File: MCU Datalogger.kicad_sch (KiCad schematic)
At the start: 25 parts, among them U1 24LC1025, U2 24LC1025, U3 DS1337S+, U4 ATMEGA328P-AU, Y1 32.768KHz, Y2 16MHz

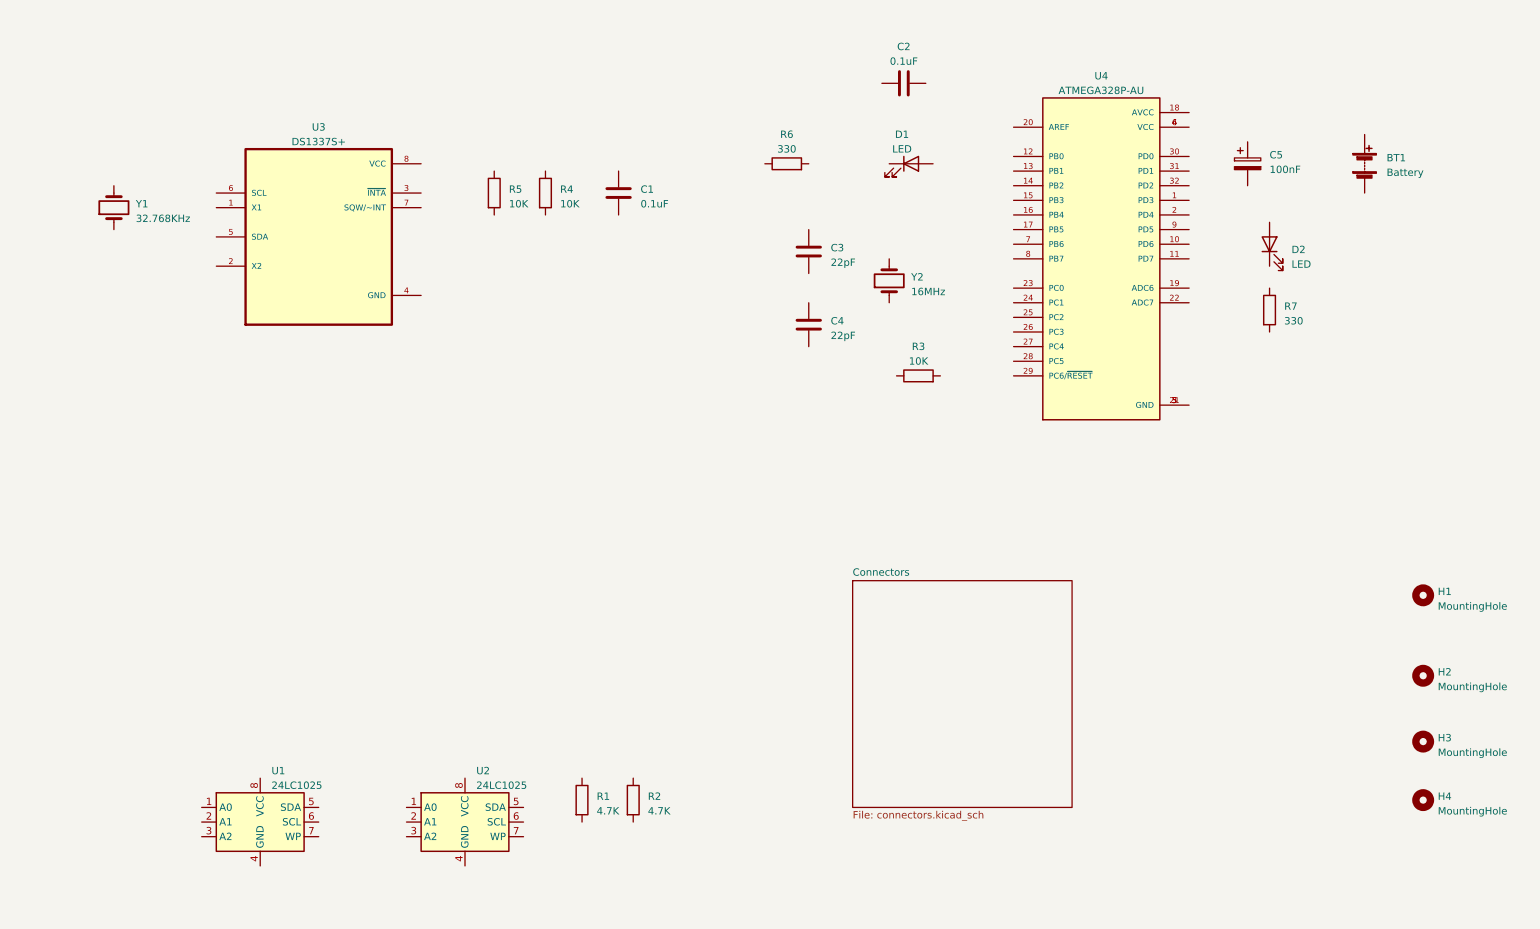
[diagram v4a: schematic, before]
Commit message: Completed wiring of main sheet
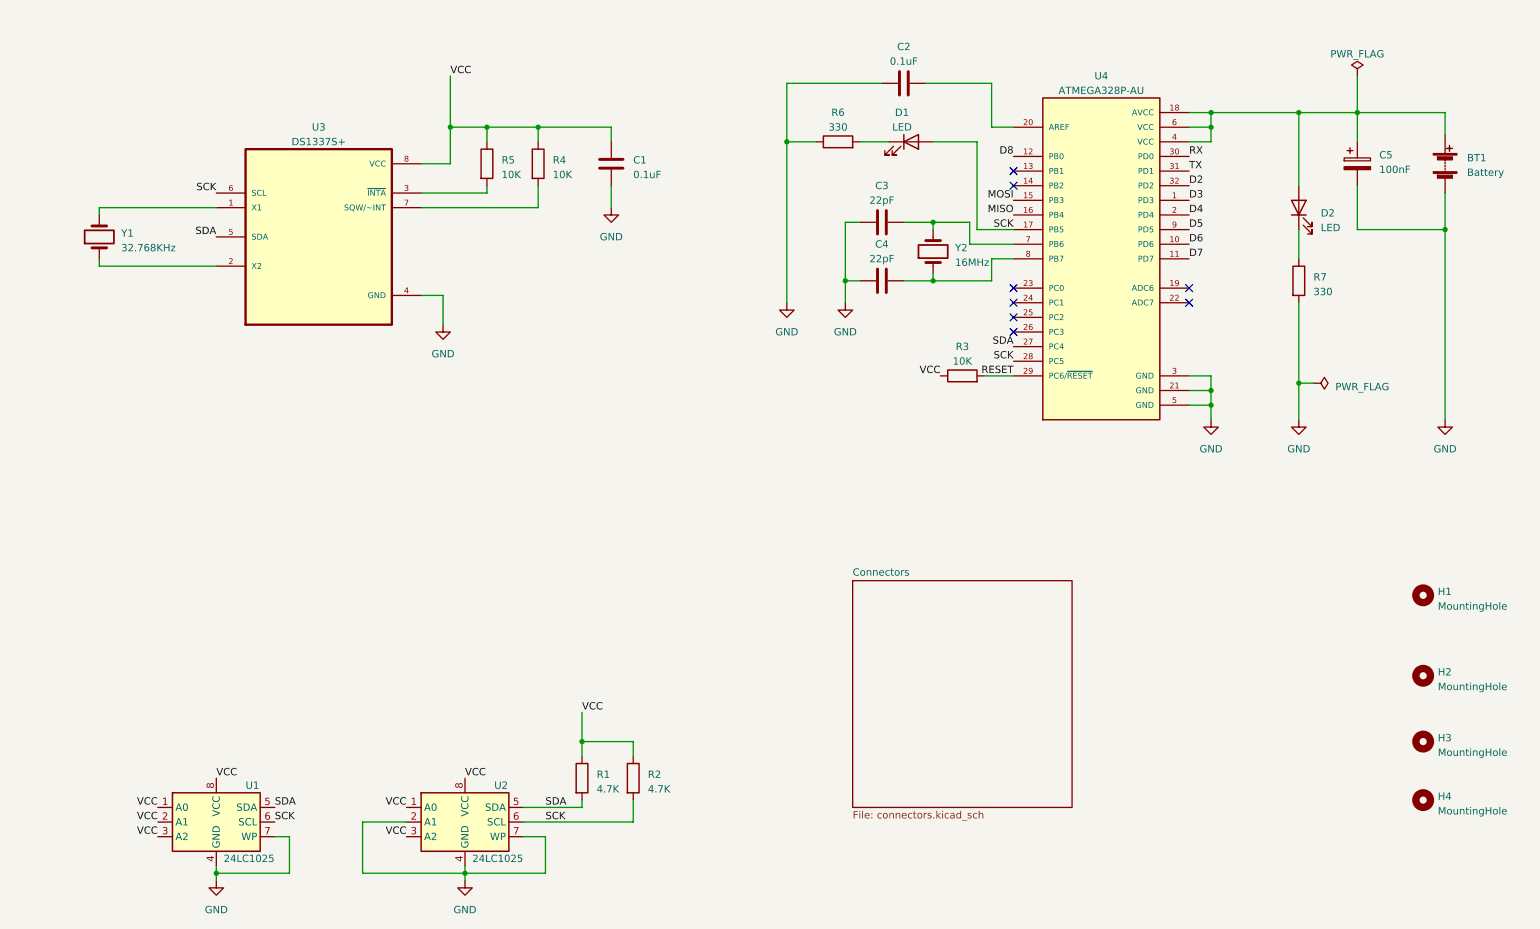
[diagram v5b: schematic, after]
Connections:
- net VCC: now reaches R5.1
- net VCC: now also C1.1, R1.1, R2.1, R3.1, R4.1, U1.1 (A0), U1.2 (A1), U1.3 (A2), U1.8 (VCC), U2.1 (A0), U2.3 (A2), U2.8 (VCC), U3.8 (VCC)
- net at R5.2: now also U3.3 (~{INTA})
- net GND: now reaches C3.1
- net GND: now also BT1.2 (-), C1.2, C2.1, C4.1, C5.2, R6.1, R7.2, U1.4 (GND), U1.7 (WP), U2.2 (A1), U2.4 (GND), U2.7 (WP), U3.4 (GND), U4.21 (GND), U4.3 (GND), U4.5 (GND)
- net at C3.2: now also U4.7 (PB6), Y2.2
- net at R7.1: now also D2.1 (K)
- net at D2.2 (A): now also BT1.1 (+), C5.1, U4.18 (AVCC), U4.4 (VCC), U4.6 (VCC)
- net SDA: now reaches R1.2
- net SDA: now also U1.5 (SDA), U2.5 (SDA), U3.5 (SDA), U4.27 (PC4)
- net SCK: now reaches R2.2
- net SCK: now also D1.2 (A), U1.6 (SCL), U2.6 (SCL), U3.6 (SCL), U4.17 (PB5), U4.28 (PC5)
- net at D1.1 (K): now also R6.2
- net at Y1.1: now also U3.2 (X2)
- net at Y1.2: now also U3.1 (X1)
- net at U3.7 (SQW/~INT): now also R4.2
- net RESET: now reaches R3.2
- net RESET: now also U4.29 (PC6/~{RESET})
- net D3: now reaches U4.1 (PD3)
- net D6: now reaches U4.10 (PD6)
- net D7: now reaches U4.11 (PD7)
- net D8: now reaches U4.12 (PB0)
- net MOSI: now reaches U4.15 (PB3)
- net MISO: now reaches U4.16 (PB4)
- net D4: now reaches U4.2 (PD4)
- net at U4.20 (AREF): now also C2.2
- net RX: now reaches U4.30 (PD0)
- net TX: now reaches U4.31 (PD1)
- net D2: now reaches U4.32 (PD2)
- net at U4.8 (PB7): now also C4.2, Y2.1
- net D5: now reaches U4.9 (PD5)
- no-connect marks 0 -> 8
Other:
- moved on the sheet: BT1, C1, C3, C4, C5, D1, D2, R1, R2, R3, R4, R5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

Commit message: Completed wiring in the second sheet.
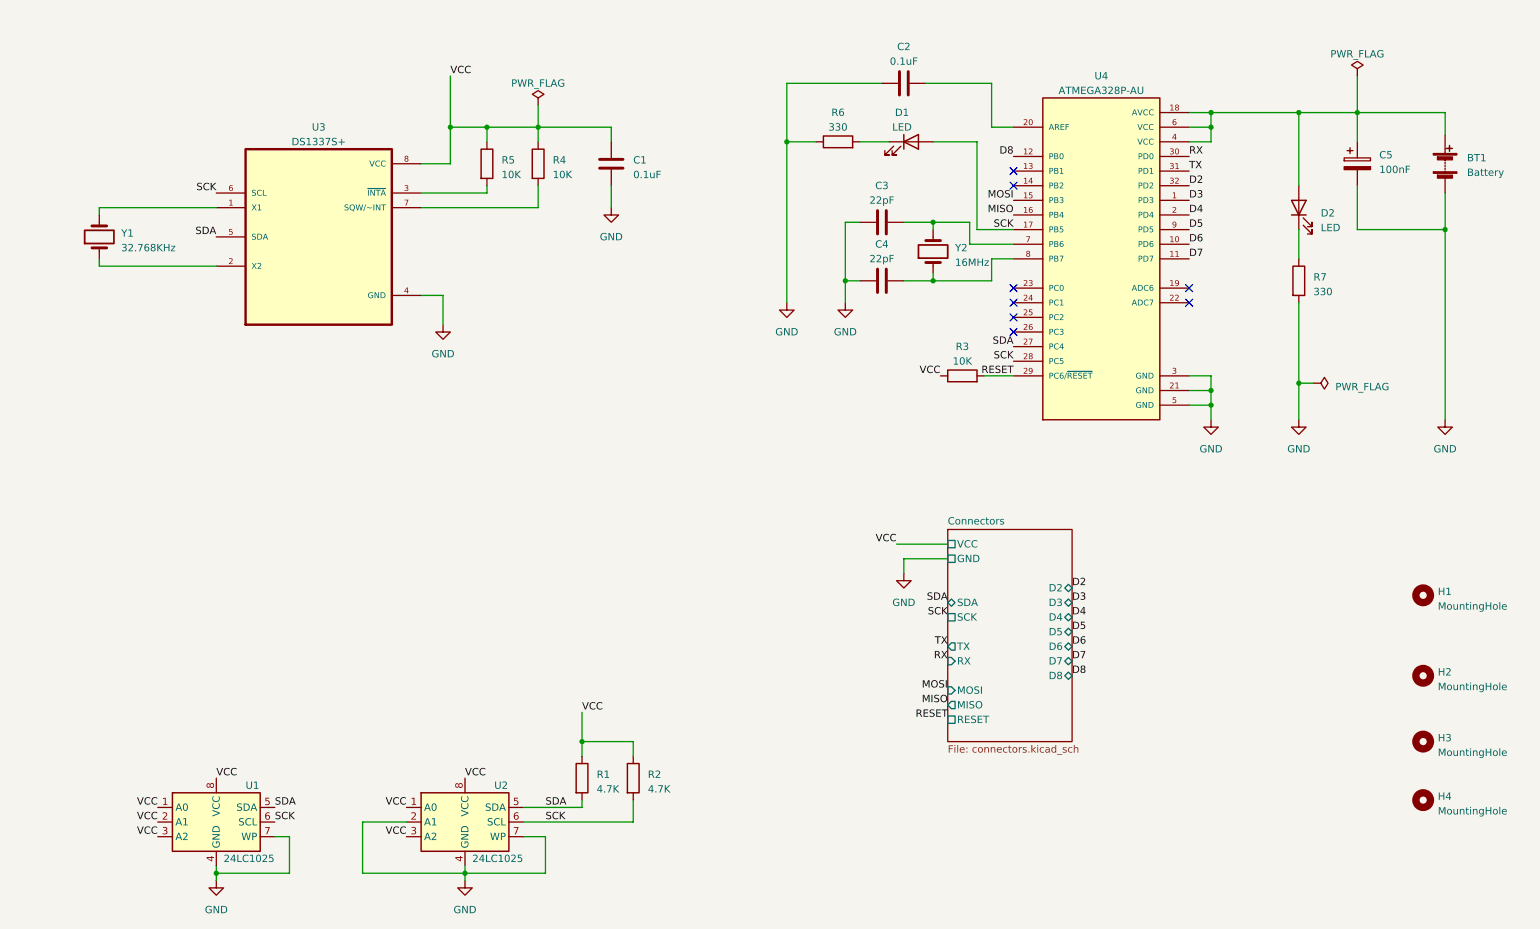
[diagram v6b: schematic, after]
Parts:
- U4: footprint Footprints:QFP80P900X900X120-32N -> QFP80P900X900X120-32N
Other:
- sheet Connectors ports: added D2, D3, D4, D5, D6, D7, D8, GND, MISO, MOSI, RESET, RX, SCK, SDA, TX, VCC; removed none
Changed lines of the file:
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@@
+    (stroke (width 0) (type default))
+  )
+  (wire (pts (xy 109.22 33.02) (xy 109.22 36.83))
     (stroke (width 0) (type default))
   )
@@
     (stroke (width 0) (type default))
   )
+  (wire (pts (xy 88.9 43.18) (xy 93.98 43.18))
+    (stroke (width 0) (type default))
+  )
   (wire (pts (xy 226.06 34.29) (xy 222.25 34.29))
     (stroke (width 0) (type default))
@@
     (stroke (width 0) (type default))
   )
+  (wire (pts (xy 172.72 111.76) (xy 172.72 114.3))
+    (stroke (width 0) (type default))
+  )
   (wire (pts (xy 241.3 34.29) (xy 226.06 34.29))
     (stroke (width 0) (type default))
@@
     (stroke (width 0) (type default))
   )
+  (wire (pts (xy 180.34 111.76) (xy 172.72 111.76))
+    (stroke (width 0) (type default))
+  )
   (wire (pts (xy 106.68 160.02) (xy 110.49 160.02))
     (stroke (width 0) (type default))
@@
     (stroke (width 0) (type default))
   )
-  (wire (pts (xy 88.9 43.18) (xy 93.98 43.18))
-    (stroke (width 0) (type default))
-  )
   (wire (pts (xy 152.4 29.21) (xy 152.4 39.37))
     (stroke (width 0) (type default))
@@
     (stroke (width 0) (type default))
   )
+  (wire (pts (xy 171.45 109.22) (xy 180.34 109.22))
+    (stroke (width 0) (type default))
+  )
   (wire (pts (xy 33.02 50.8) (xy 33.02 52.07))
     (stroke (width 0) (type default))
@@
     (stroke (width 0) (type default))
   )
+  (label "MOSI" (at 180.34 134.62 180) (fields_autoplaced)
+    (effects (font (size 1.27 1.27)) (justify right bottom))
+  )
   (label "D2" (at 222.25 46.99 0) (fields_autoplaced)
     (effects (font (size 1.27 1.27)) (justify left bottom))
@@
     (effects (font (size 1.27 1.27)) (justify right bottom))
   )
+  (label "VCC" (at 171.45 109.22 180) (fields_autoplaced)
+    (effects (font (size 1.27 1.27)) (justify right bottom))
+  )
   (label "SCK" (at 191.77 54.61 180) (fields_autoplaced)
     (effects (font (size 1.27 1.27)) (justify right bottom))
@@
     (effects (font (size 1.27 1.27)) (justify right bottom))
   )
+  (label "D7" (at 201.93 129.54 0) (fields_autoplaced)
+    (effects (font (size 1.27 1.27)) (justify left bottom))
+  )
   (label "SDA" (at 110.49 154.94 0) (fields_autoplaced)
     (effects (font (size 1.27 1.27)) (justify left bottom))
   )
+  (label "D3" (at 201.93 119.38 0) (fields_autoplaced)
+    (effects (font (size 1.27 1.27)) (justify left bottom))
+  )
   (label "RESET" (at 191.77 80.01 180) (fields_autoplaced)
     (effects (font (size 1.27 1.27)) (justify right bottom))
@@
     (effects (font (size 1.27 1.27)) (justify right bottom))
   )
+  (label "RX" (at 180.34 129.54 180) (fields_autoplaced)
+    (effects (font (size 1.27 1.27)) (justify right bottom))
+  )
   (label "RX" (at 222.25 41.91 0) (fields_autoplaced)
     (effects (font (size 1.27 1.27)) (justify left bottom))
@@
     (effects (font (size 1.27 1.27)) (justify left bottom))
   )
+  (label "D2" (at 201.93 116.84 0) (fields_autoplaced)
+    (effects (font (size 1.27 1.27)) (justify left bottom))
+  )
   (label "SDA" (at 63.5 154.94 0) (fields_autoplaced)
     (effects (font (size 1.27 1.27)) (justify left bottom))
@@
     (effects (font (size 1.27 1.27)) (justify left bottom))
   )
+  (label "D6" (at 201.93 127 0) (fields_autoplaced)
+    (effects (font (size 1.27 1.27)) (justify left bottom))
+  )
   (label "SCK" (at 63.5 157.48 0) (fields_autoplaced)
     (effects (font (size 1.27 1.27)) (justify left bottom))
@@
     (effects (font (size 1.27 1.27)) (justify right bottom))
   )
+  (label "SCK" (at 180.34 121.92 180) (fields_autoplaced)
+    (effects (font (size 1.27 1.27)) (justify right bottom))
+  )
   (label "VCC" (at 53.34 149.86 0) (fields_autoplaced)
     (effects (font (size 1.27 1.27)) (justify left bottom))
   )
+  (label "SDA" (at 180.34 119.38 180) (fields_autoplaced)
+    (effects (font (size 1.27 1.27)) (justify right bottom))
+  )
+  (label "D5" (at 201.93 124.46 0) (fields_autoplaced)
+    (effects (font (size 1.27 1.27)) (justify left bottom))
+  )
+  (label "D8" (at 201.93 132.08 0) (fields_autoplaced)
+    (effects (font (size 1.27 1.27)) (justify left bottom))
+  )
+  (label "RESET" (at 180.34 139.7 180) (fields_autoplaced)
+    (effects (font (size 1.27 1.27)) (justify right bottom))
+  )
+  (label "D4" (at 201.93 121.92 0) (fields_autoplaced)
+    (effects (font (size 1.27 1.27)) (justify left bottom))
+  )
   (label "D5" (at 222.25 54.61 0) (fields_autoplaced)
     (effects (font (size 1.27 1.27)) (justify left bottom))
@@
     (effects (font (size 1.27 1.27)) (justify right bottom))
   )
+  (label "MISO" (at 180.34 137.16 180) (fields_autoplaced)
+    (effects (font (size 1.27 1.27)) (justify right bottom))
+  )
+  (label "TX" (at 180.34 127 180) (fields_autoplaced)
+    (effects (font (size 1.27 1.27)) (justify right bottom))
+  )
   (label "VCC" (at 179.07 80.01 180) (fields_autoplaced)
     (effects (font (size 1.27 1.27)) (justify right bottom))
@@
         (path "/a2e2aee7-f3a1-41aa-a08b-33521bd80092"
           (reference "C3") (unit 1)
+        )
+      )
+    )
+  )
+  (symbol (lib_id "power:PWR_FLAG") (at 109.22 33.02 0) (unit 1)
+    (in_bom yes) (on_board yes) (dnp no) (fields_autoplaced)
+    (property "Reference" "#FLG03" (at 109.22 31.115 0)
+      (effects (font (size 1.27 1.27)) hide)
+    )
+    (property "Value" "PWR_FLAG" (at 109.22 29.21 0)
+      (effects (font (size 1.27 1.27)))
+    )
+    (property "Footprint" "" (at 109.22 33.02 0)
+      (effects (font (size 1.27 1.27)) hide)
+    )
+    (property "Datasheet" "~" (at 109.22 33.02 0)
+      (effects (font (size 1.27 1.27)) hide)
+    )
+    (pin "1")
+    (instances
+      (project "MCU Datalogger"
+        (path "/a2e2aee7-f3a1-41aa-a08b-33521bd80092"
+          (reference "#FLG03") (unit 1)
         )
       )
@@
         (path "/a2e2aee7-f3a1-41aa-a08b-33521bd80092"
           (reference "R1") (unit 1)
+        )
+      )
+    )
+  )
+  (symbol (lib_id "power:GND") (at 172.72 114.3 0) (unit 1)
+    (in_bom yes) (on_board yes) (dnp no) (fields_autoplaced)
+    (property "Reference" "#PWR010" (at 172.72 120.65 0)
+      (effects (font (size 1.27 1.27)) hide)
+    )
+    (property "Value" "GND" (at 172.72 119.38 0)
+      (effects (font (size 1.27 1.27)))
+    )
+    (property "Footprint" "" (at 172.72 114.3 0)
+      (effects (font (size 1.27 1.27)) hide)
+    )
+    (property "Datasheet" "" (at 172.72 114.3 0)
+      (effects (font (size 1.27 1.27)) hide)
+    )
+    (pin "1")
+    (instances
+      (project "MCU Datalogger"
+        (path "/a2e2aee7-f3a1-41aa-a08b-33521bd80092"
+          (reference "#PWR010") (unit 1)
         )
       )
@@
       (effects (font (size 1.27 1.27)))
     )
-    (property "Footprint" "Footprints:QFP80P900X900X120-32N" (at 207.01 59.69 0)
+    (property "Footprint" "QFP80P900X900X120-32N" (at 207.01 59.69 0)
       (effects (font (size 1.27 1.27)) (justify bottom) hide)
     )
@@
     )
   )
-  (sheet (at 163.83 115.57) (size 38.1 39.37) (fields_autoplaced)
+  (sheet (at 180.34 106.68) (size 21.59 36.83) (fields_autoplaced)
     (stroke (width 0.1524) (type solid))
     (fill (color 0 0 0 0.0000))
-    (property "Sheetname" "Connectors" (at 163.83 114.8584 0)
+    (property "Sheetname" "Connectors" (at 180.34 105.9684 0)
       (effects (font (size 1.27 1.27)) (justify left bottom))
     )
-    (property "Sheetfile" "connectors.kicad_sch" (at 163.83 155.5246 0)
+    (property "Sheetfile" "connectors.kicad_sch" (at 180.34 144.0946 0)
       (effects (font (size 1.27 1.27)) (justify left top))
     )
-    (instances
+    (pin "SCK" passive (at 180.34 121.92 180)
+      (effects (font (size 1.27 1.27)) (justify left))
+    )
+    (pin "GND" passive (at 180.34 111.76 180)
+      (effects (font (size 1.27 1.27)) (justify left))
+    )
+    (pin "VCC" passive (at 180.34 109.22 180)
+      (effects (font (size 1.27 1.27)) (justify left))
+    )
+    (pin "SDA" bidirectional (at 180.34 119.38 180)
+      (effects (font (size 1.27 1.27)) (justify left))
+    )
+    (pin "D5" bidirectional (at 201.93 124.46 0)
+      (effects (font (size 1.27 1.27)) (justify right))
+    )
+    (pin "D8" bidirectional (at 201.93 132.08 0)
+      (effects (font (size 1.27 1.27)) (justify right))
+    )
+    (pin "D3" bidirectional (at 201.93 119.38 0)
+      (effects (font (size 1.27 1.27)) (justify right))
+    )
+    (pin "D2" bidirectional (at 201.93 116.84 0)
+      (effects (font (size 1.27 1.27)) (justify right))
+    )
+    (pin "D4" bidirectional (at 201.93 121.92 0)
+      (effects (font (size 1.27 1.27)) (justify right))
+    )
+    (pin "TX" output (at 180.34 127 180)
+      (effects (font (size 1.27 1.27)) (justify left))
+    )
+    (pin "RX" input (at 180.34 129.54 180)
+      (effects (font (size 1.27 1.27)) (justify left))
+    )
+    (pin "D6" bidirectional (at 201.93 127 0)
+      (effects (font (size 1.27 1.27)) (justify right))
+    )
+    (pin "D7" bidirectional (at 201.93 129.54 0)
+      (effects (font (size 1.27 1.27)) (justify right))
+    )
+    (pin "MOSI" input (at 180.34 134.62 180)
+      (effects (font (size 1.27 1.27)) (justify left))
+    )
+    (pin "MISO" output (at 180.34 137.16 180)
+      (effects (font (size 1.27 1.27)) (justify left))
+    )
+    (pin "RESET" passive (at 180.34 139.7 180)
+      (effects (font (size 1.27 1.27)) (justify left))
+    )
+    (instances

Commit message: Completed comments
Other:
- note added: "CONNECTORS"
- note added: "EEPROM"
- note added: "MCU"
- note added: "MOUNTING"
- note added: "Real Time Clock"
- moved on the sheet: H1, H2, H3, H4, R1, R2, U1, U2
